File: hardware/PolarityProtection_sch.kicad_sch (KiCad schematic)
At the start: 18 parts, among them IC1 LM74502HDDFR, Q1 NVMFWS1D7N04XMT1G, Q4 NVMFWS1D7N04XMT1G

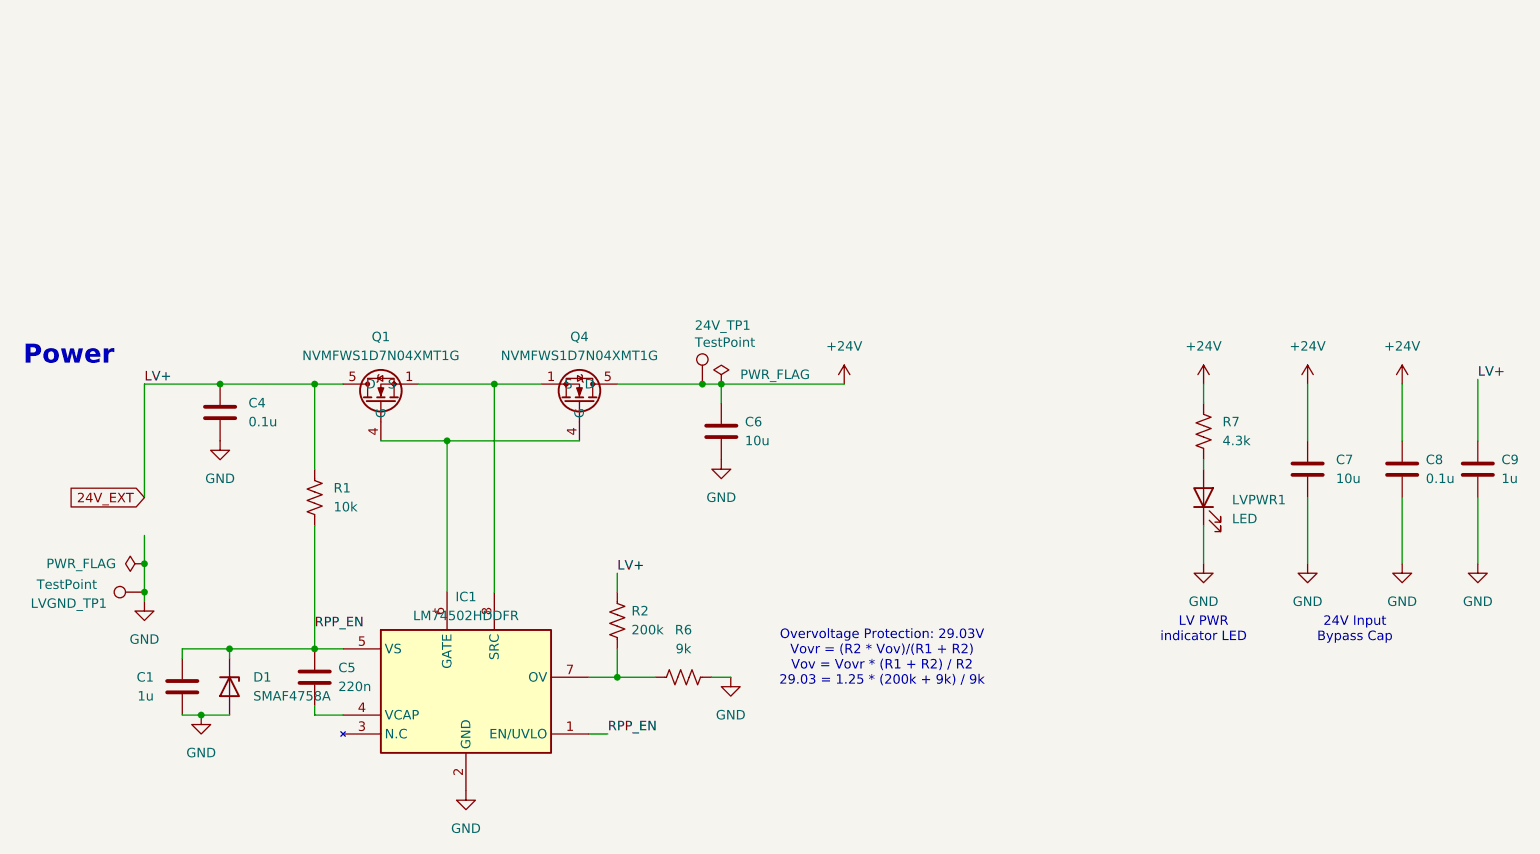
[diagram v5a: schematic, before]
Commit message: Switched MX150 to 02x05 nanofet
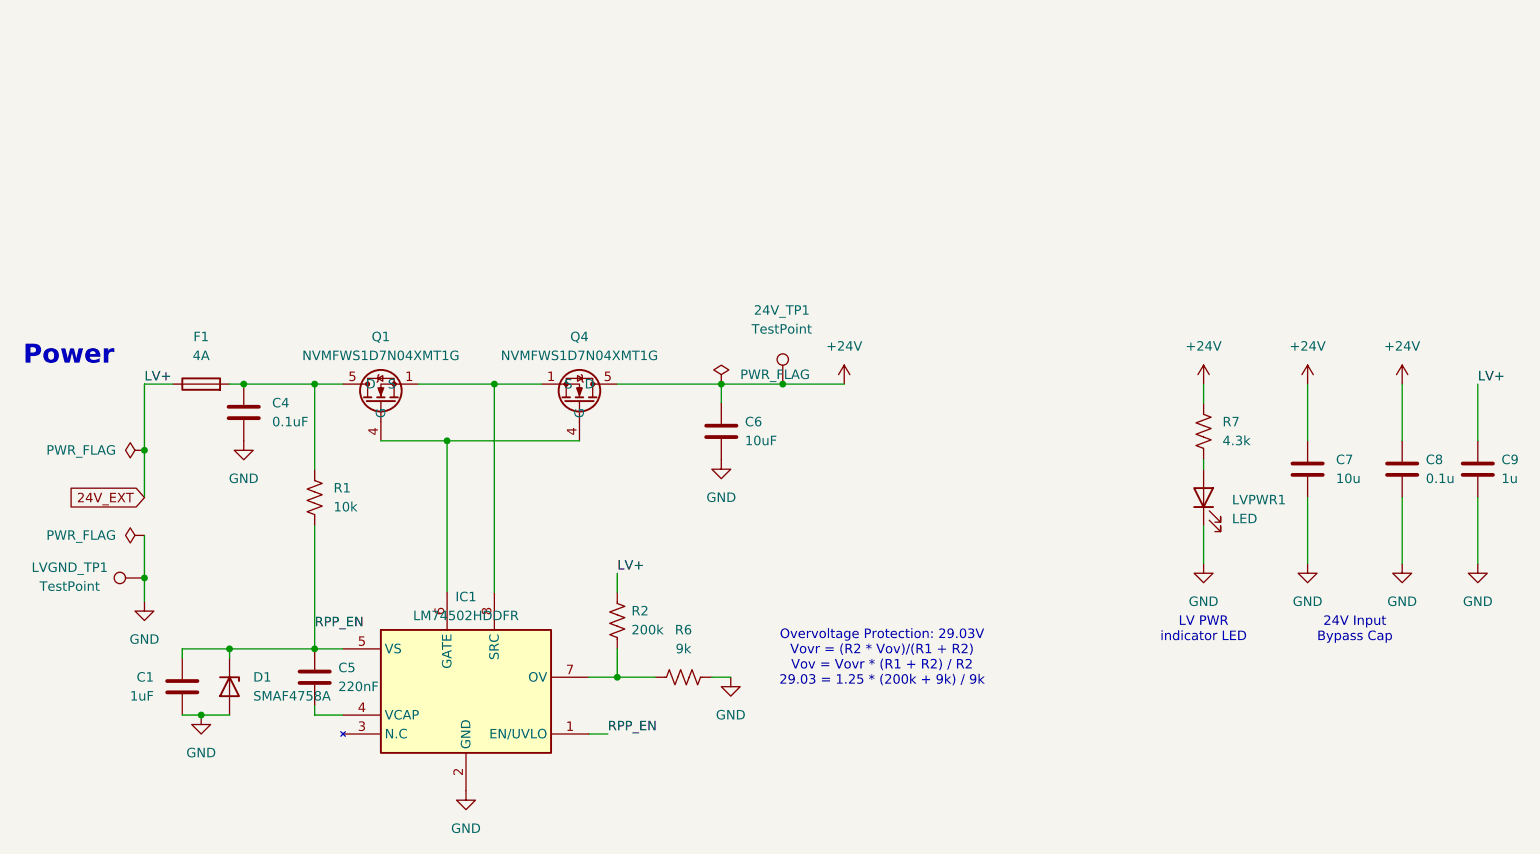
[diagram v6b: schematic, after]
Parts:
- added F1: 4A, UTSVT_Connectors:FUSE_3568, symbol UTSVT-Power:Fuse_3568
- 24V_TP1, LVGND_TP1: footprint TestPoint:TestPoint_Keystone_5005-5009_Compact -> UTSVT_Special:TestPoint_HEX_3mmID; now in the parts list
- C1: value 1u -> 1uF; footprint Capacitor_SMD:C_0603_1608Metric_Pad1.08x0.95mm_HandSolder -> Capacitor_SMD:C_0603_1608Metric
- C4: value 0.1u -> 0.1uF; footprint Capacitor_SMD:C_0603_1608Metric_Pad1.08x0.95mm_HandSolder -> Capacitor_SMD:C_0603_1608Metric
- C5: value 220n -> 220nF; footprint Capacitor_SMD:C_0603_1608Metric_Pad1.08x0.95mm_HandSolder -> Capacitor_SMD:C_0603_1608Metric
- C6: value 10u -> 10uF; footprint Capacitor_SMD:C_0805_2012Metric_Pad1.18x1.45mm_HandSolder -> Capacitor_SMD:C_0603_1608Metric
- C7: footprint Capacitor_SMD:C_0805_2012Metric_Pad1.18x1.45mm_HandSolder -> Capacitor_SMD:C_0603_1608Metric
- C8, C9: footprint Capacitor_SMD:C_0603_1608Metric_Pad1.08x0.95mm_HandSolder -> Capacitor_SMD:C_0603_1608Metric
- R1, R2, R6, R7: footprint Resistor_SMD:R_0603_1608Metric_Pad0.98x0.95mm_HandSolder -> Resistor_SMD:R_0603_1608Metric
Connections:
- net 24V_EXT: now also F1.1; no longer C4.1, Q1.5 (D), Q1.6 (D), Q1.7 (D), Q1.8 (D), Q1.9 (D), R1.1
- new net: C4.1, F1.2, Q1.5 (D), Q1.6 (D), Q1.7 (D), Q1.8 (D), Q1.9 (D), R1.1
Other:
- moved on the sheet: C4

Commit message: Current Layout
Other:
- moved on the sheet: 24V_TP1, C4, LVGND_TP1
